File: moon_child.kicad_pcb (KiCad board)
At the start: 4 copper layers, 63.2 x 63.2 mm, 191 parts, among them J1 Motor0, J10 USB_C_Receptacle_USB2.0_14P, J2 Motor1, J3 Battery Input, J4 Micro_SD_Card_Det1, J5 Conn_01x04, J6 Conn_01x04, J7 Conn_02x05_Odd_Even, J8 Conn_01x03, J9 debug_probe, Q1 BSP613P, Q2 Q_NPN_BCE, SW1 SW_Omron_B3FS, U1 DRV8871DDA, U2 DRV8871DDA, U3 AP62250Z6, U4 IIM-42652, U5 BME280, U6 RP2350B-QFN80, U7 INA180A1, U8 16Mbit PSRAM, U9 16Mbit PSRAM, X1 ASE-12.000MHZ-L-C-T

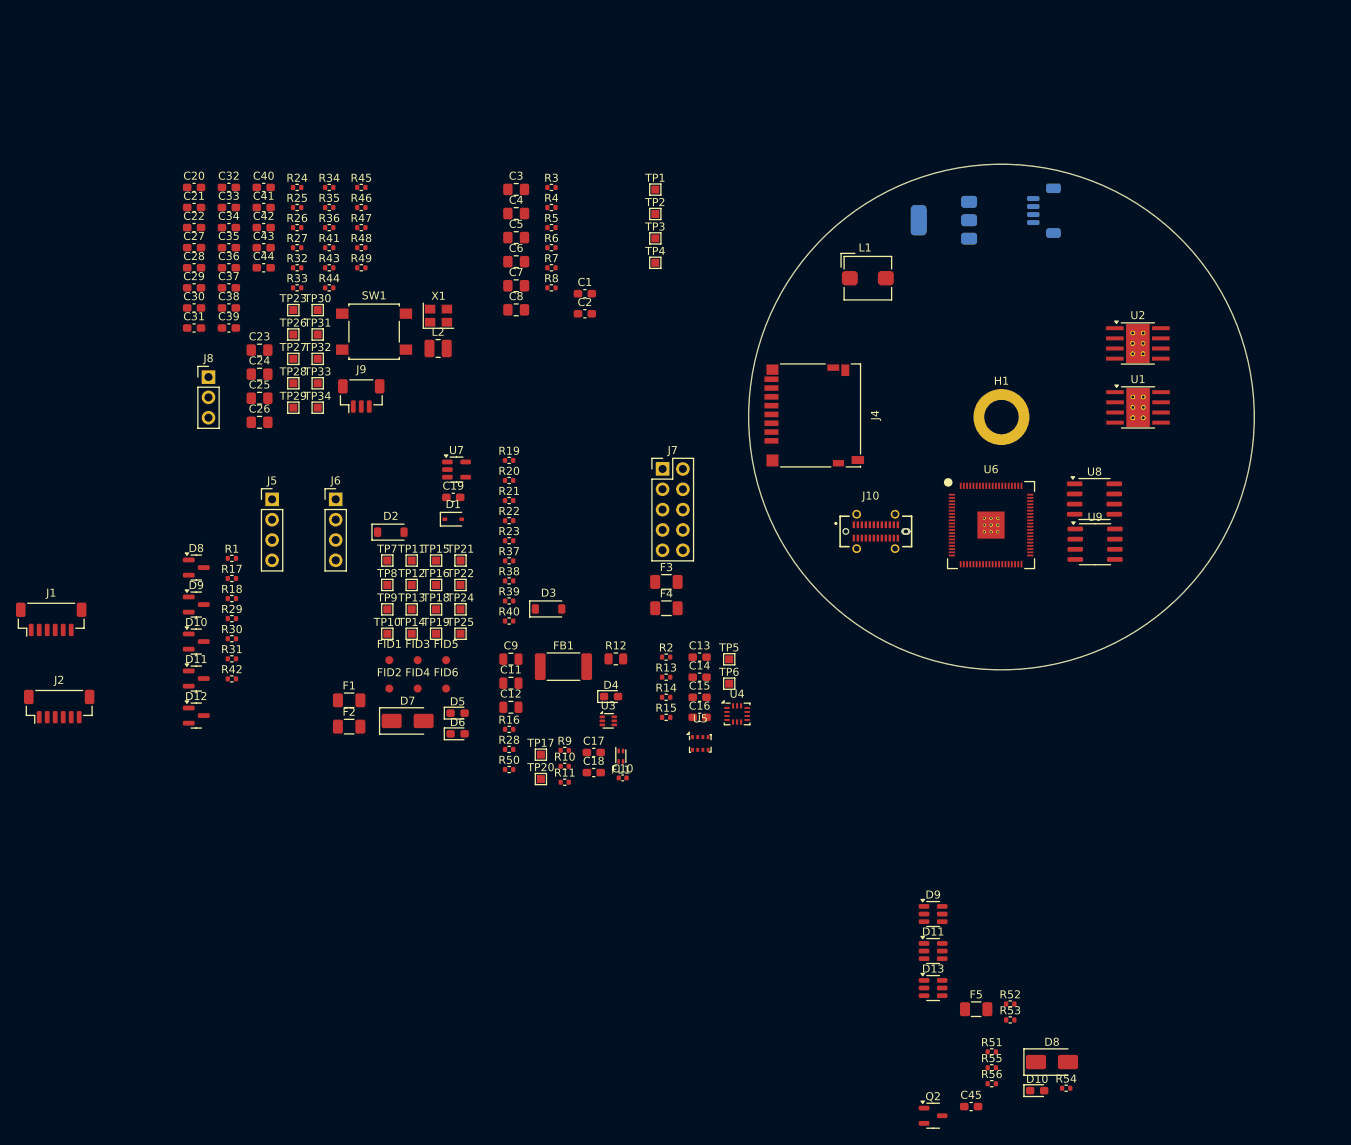
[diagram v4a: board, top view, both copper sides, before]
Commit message: Swapped motor polarity
Swapped motor polarity for easier routing + other component positioning.
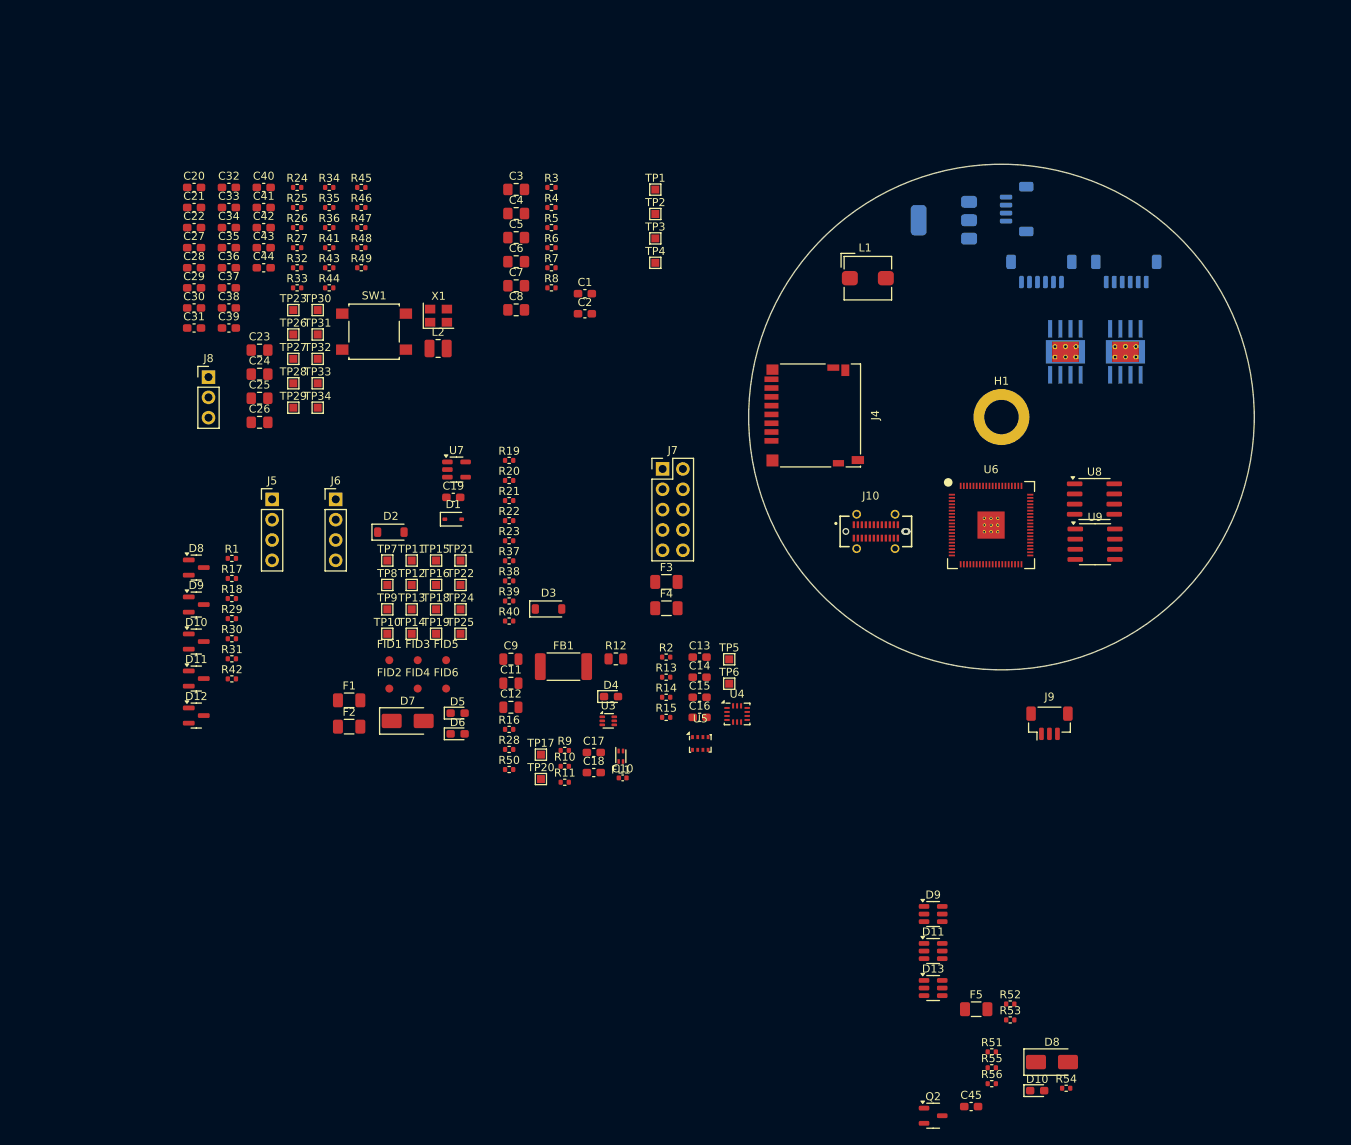
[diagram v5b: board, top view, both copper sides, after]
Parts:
- J1, J2, U1, U2: moved to B.Cu
- moved J2 144.0 mm to (174.8, 70.3), turned to 180 degrees
- moved J1 131.2 mm to (164.2, 70.3), turned to 180 degrees
- moved J9 95.3 mm to (165.2, 126.8)
- moved U2 9.11 mm to (167.2, 80.3), turned to 90 degrees
- moved U1 7.12 mm to (174.7, 80.3), turned to 90 degrees
- moved J3 3.41 mm to (161.1, 62.5)
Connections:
- U1 pad 6: Motor0_+ -> Motor0_-
- U1 pad 8: Motor0_- -> Motor0_+
- U2 pad 6: Motor1_+ -> Motor1_-
- U2 pad 8: Motor1_- -> Motor1_+

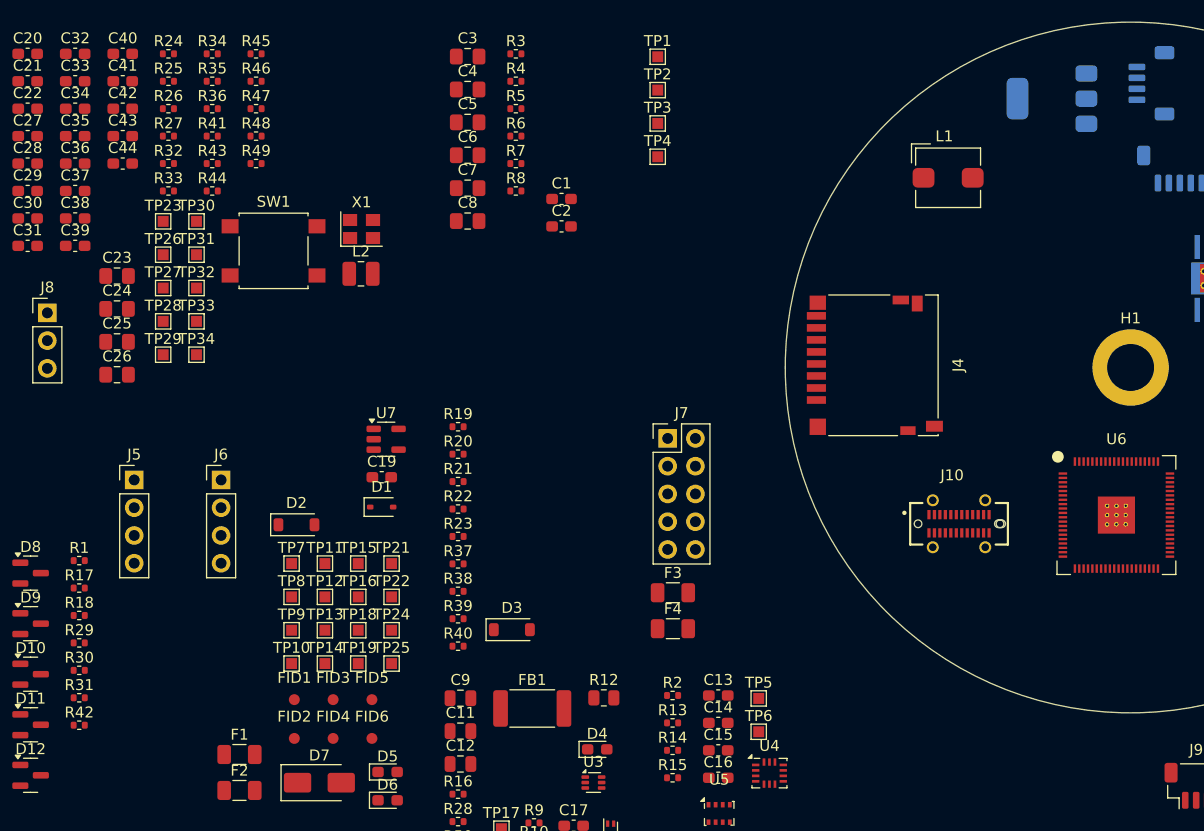
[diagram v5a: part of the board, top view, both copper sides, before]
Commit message: Updated routing
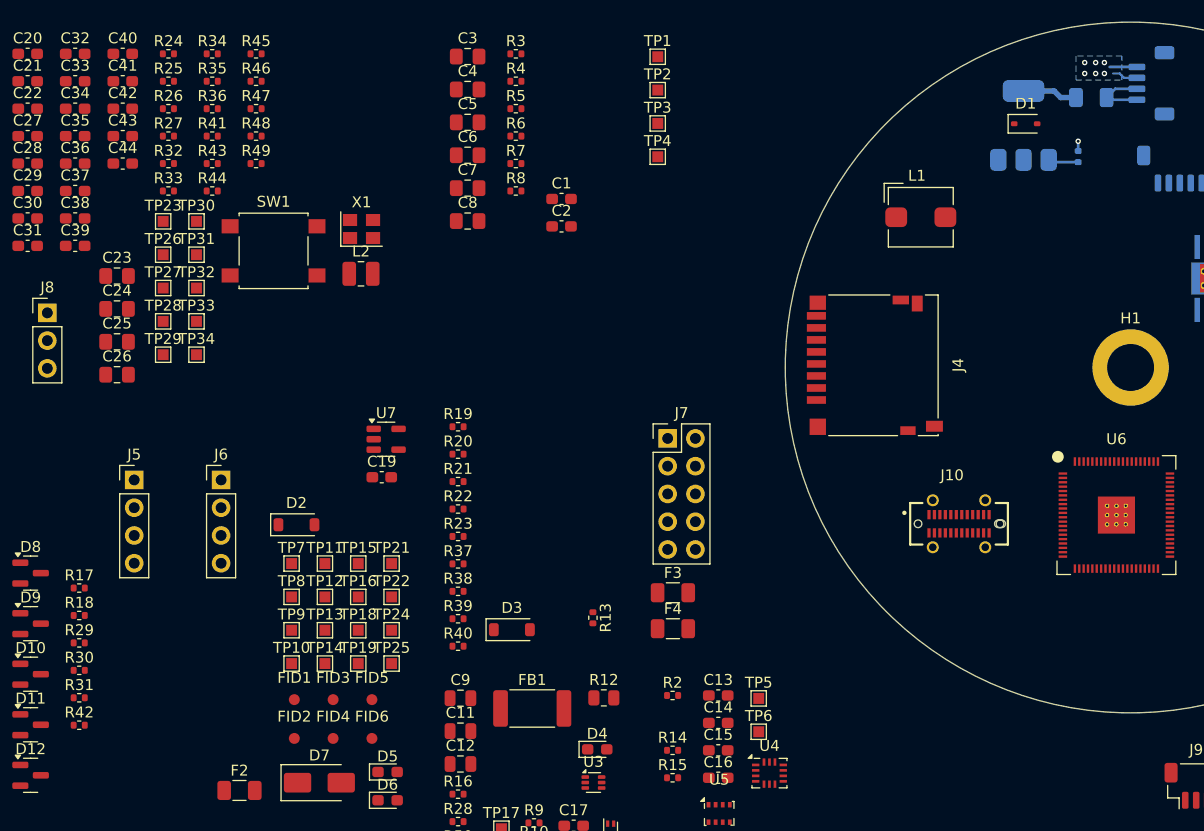
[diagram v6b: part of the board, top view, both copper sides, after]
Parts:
- F1, R1: moved to B.Cu
- moved R1 98.6 mm to (154.4, 69.2), turned to 90 degrees
- moved F1 98.4 mm to (155.6, 63.8), turned to 180 degrees
- moved D1 68.6 mm to (149.6, 66.2)
- moved R13 12.1 mm to (110.0, 111.4), turned to -90 degrees
- moved L1 4.39 mm to (140.0, 74.8)
- moved Q1 3.57 mm to (149.4, 66.3), turned to 90 degrees
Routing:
- net /connectors+mechanical/Input_Voltage: track 0.00 -> 5.96 mm
- net GND: track 0.00 -> 5.75 mm, vias 0 -> 7
- net Net-(D7-A): track 0.00 -> 5.05 mm
- net Net-(D1-A): track 0.00 -> 2.79 mm
- added copper zone on B.Cu, net GND

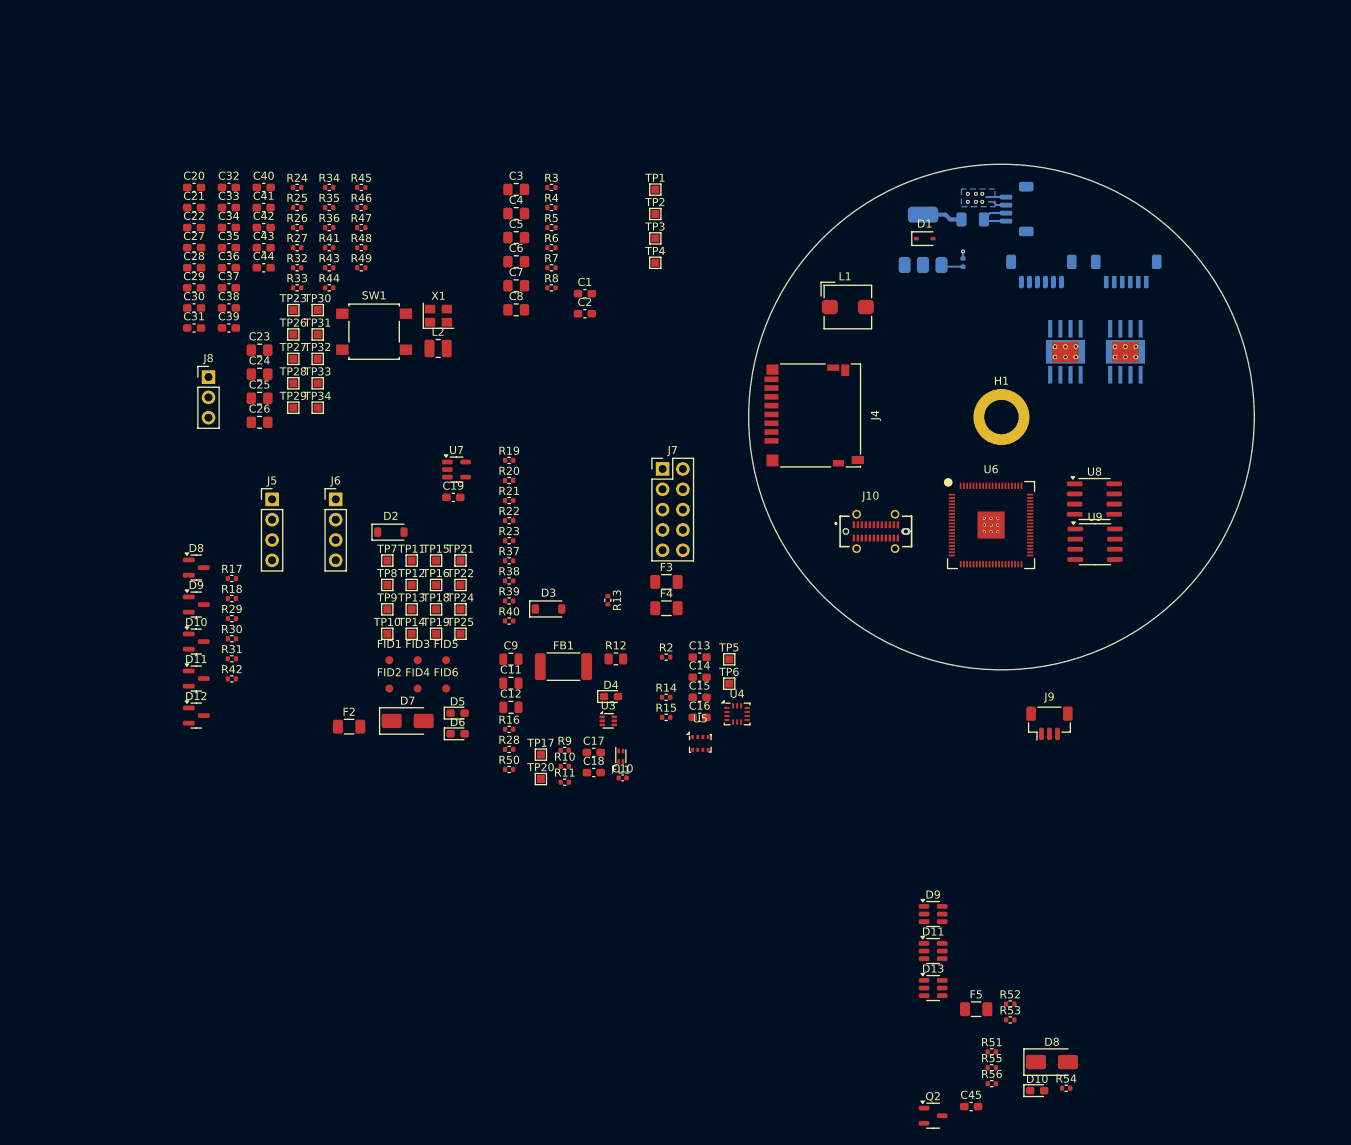
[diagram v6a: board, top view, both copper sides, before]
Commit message: Layout updates
Added 3v3 switcher layout + extras
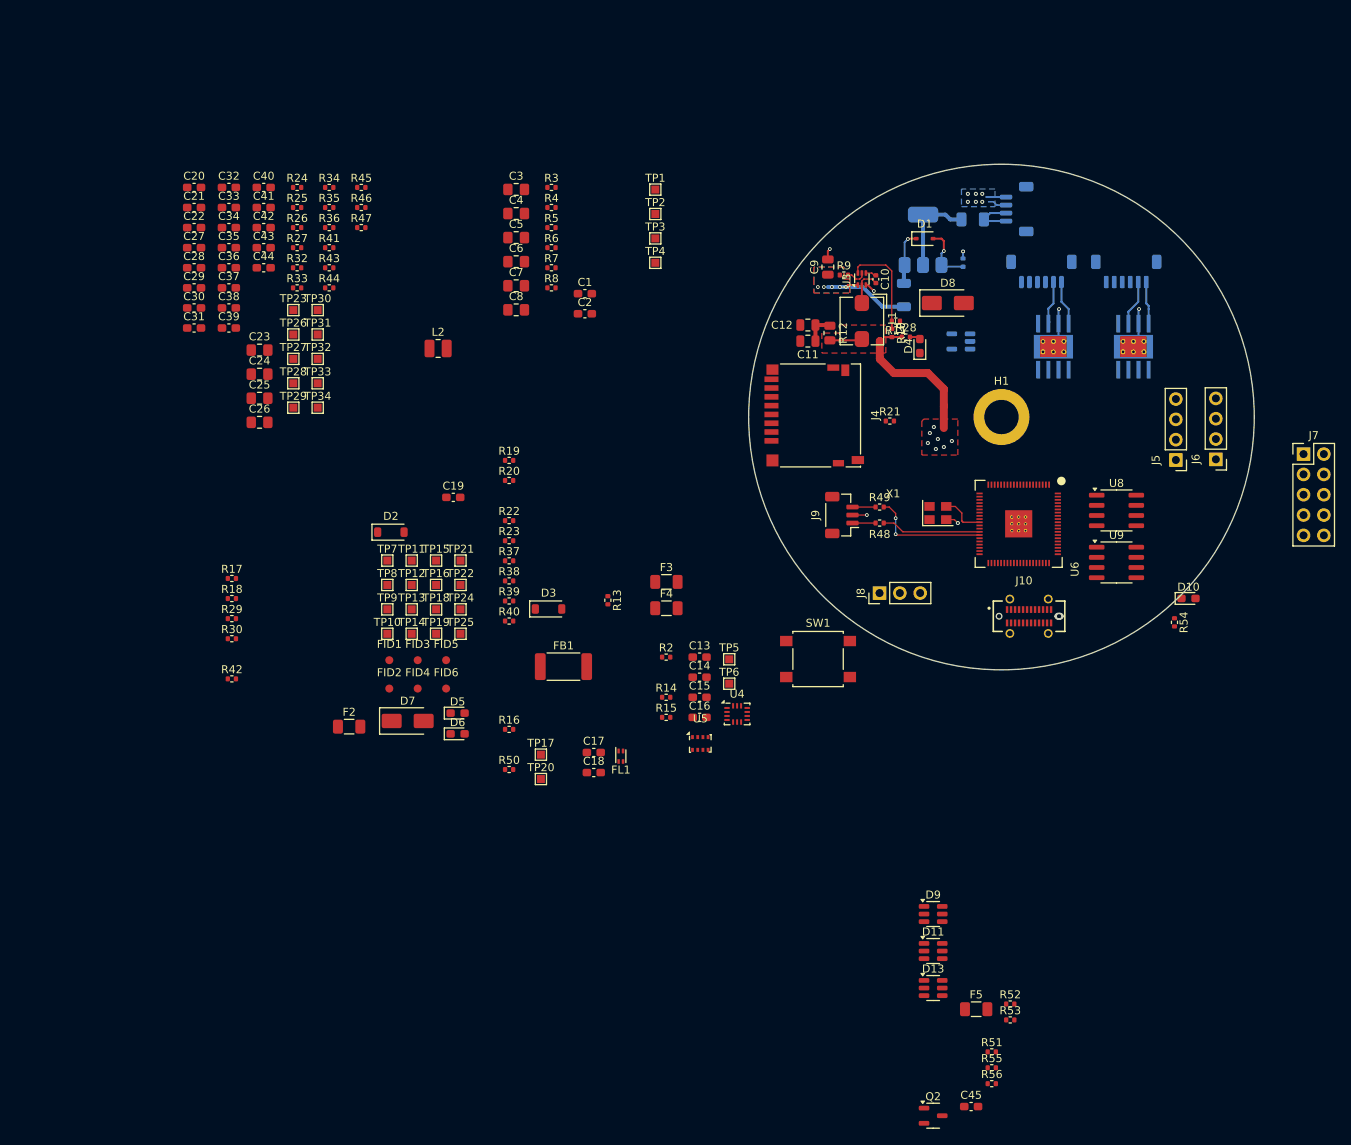
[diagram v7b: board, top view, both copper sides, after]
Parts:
- removed the D10 at (58.5, 116.6)
- removed the D11 at (58.5, 121.2)
- removed D12: SP0502BAHT, Package_TO_SOT_SMD:SOT-23
- removed the D8 at (58.5, 107.3)
- removed the D9 at (58.5, 111.9)
- R31: footprint Resistor_SMD:R_0402_1005Metric -> Resistor_SMD:R_1206_3216Metric; moved to B.Cu
- U7: moved to B.Cu
- moved J5 113.1 mm to (181.0, 93.9), turned to 180 degrees
- moved J6 110.1 mm to (186.0, 93.8), turned to 180 degrees
- moved D8 95.8 mm to (152.5, 74.2)
- moved R31 95.5 mm to (147.0, 73.2), turned to -90 degrees
- moved J8 88.1 mm to (144.0, 110.5), turned to 90 degrees
- moved J7 80.1 mm to (197.0, 93.1)
- moved R48 73.4 mm to (144.0, 101.8), turned to 180 degrees
- moved R28 71.5 mm to (147.2, 78.5)
- moved R49 71.4 mm to (144.0, 99.8), turned to 180 degrees
- moved R11 71.0 mm to (146.0, 76.5), turned to 180 degrees
- moved C10 69.9 mm to (143.5, 71.3), turned to -90 degrees
- moved SW1 69.0 mm to (136.3, 118.8)
- moved R9 68.9 mm to (139.5, 70.8)
- moved R10 67.9 mm to (145.5, 78.0), turned to -90 degrees
- moved X1 67.1 mm to (151.2, 100.5)
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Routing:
- net 3v3: track 0.00 -> 23.0 mm, vias 0 -> 7
- net GND: track 5.75 -> 23.1 mm, vias 7 -> 13
- net /raspi/SWDIO: track 0.00 -> 15.1 mm, vias 0 -> 2
- net Net-(U3-FB): track 0.00 -> 12.7 mm
- net /raspi/SWCLK: track 0.00 -> 12.4 mm
- net Board_VBATT: track 0.00 -> 12.1 mm, vias 0 -> 5
- net Net-(D1-K): track 0.00 -> 6.82 mm, vias 0 -> 1
- net Net-(D7-A): track 5.05 -> 11.3 mm
- net Motor1_-: track 0.00 -> 5.86 mm
- net Motor0_-: track 0.00 -> 5.80 mm
- net Motor0_+: track 0.00 -> 5.60 mm
- net Net-(U6-XIN): track 0.00 -> 5.56 mm
- net Motor1_+: track 0.00 -> 5.48 mm
- net Net-(D1-A): track 2.79 -> 7.39 mm, vias 0 -> 1
- net Net-(U3-SW): track 0.00 -> 4.56 mm
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- added copper zone on F.Cu, net 3v3
- added copper zone on B.Cu, net Board_VBATT
- added copper zone on F.Cu, net Board_VBATT
